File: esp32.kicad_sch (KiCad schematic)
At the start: 34 parts, among them J3 TC2030-IDC, J8 USB_C_Receptacle_USB2.0, Q3 S8050, SW1 GT-TC029B-H025-L1N, SW2 GT-TC029B-H025-L1N, U3 176x320_st7789, U7 SN74AVC4T774, U9 ESP32-S3-WROOM-1, Y1 32.768kHz

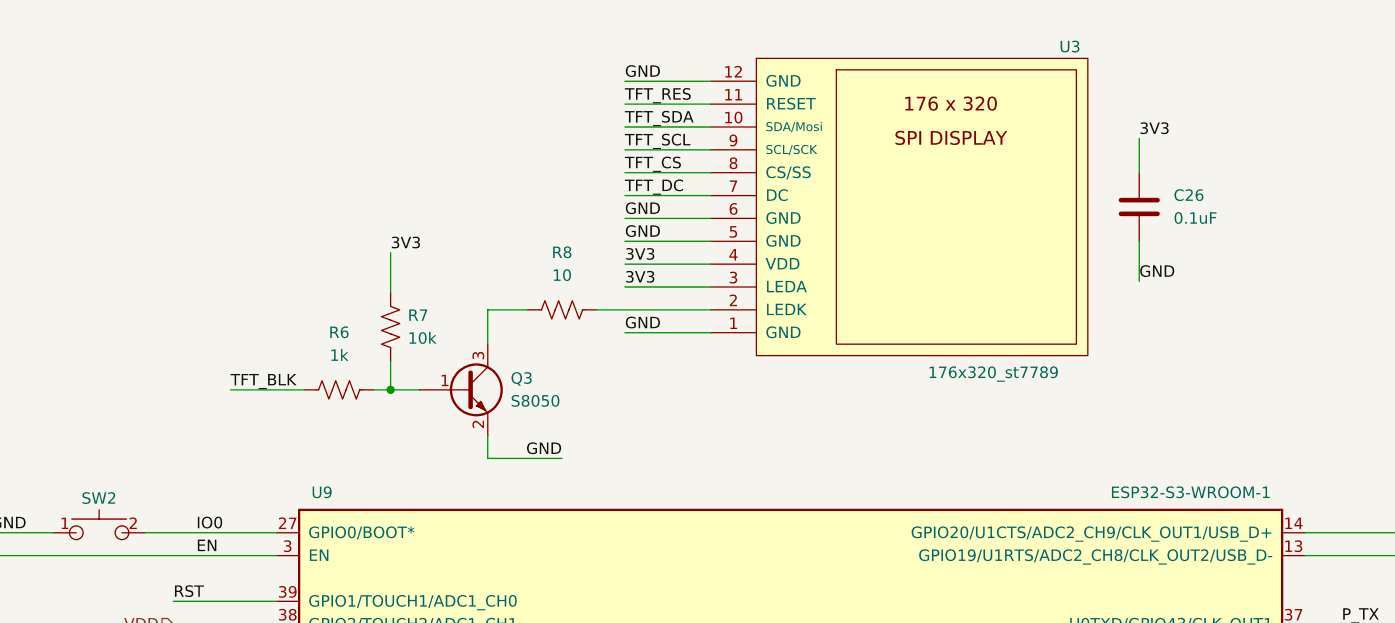
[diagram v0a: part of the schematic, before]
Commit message: replace Q5 with BSS123
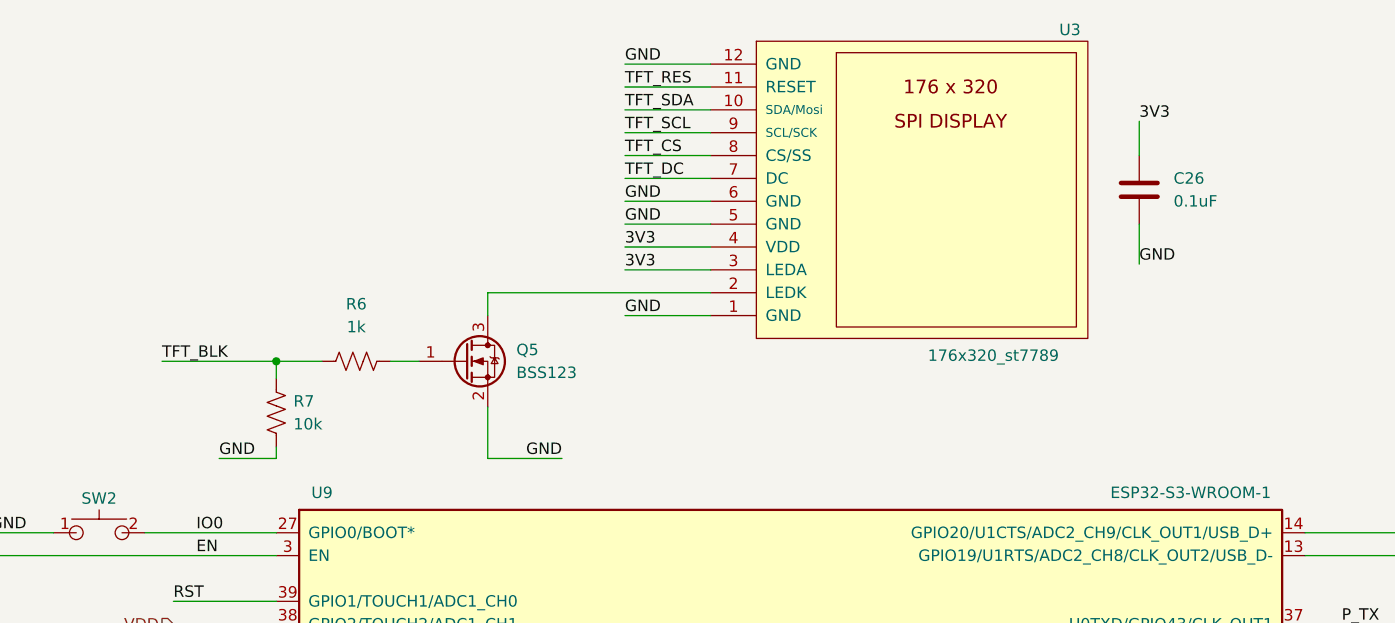
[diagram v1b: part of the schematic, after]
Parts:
- removed Q3: S8050, Package_TO_SOT_SMD:SOT-23-3, symbol Device:Q_NPN_BEC
- removed R8: 10, Resistor_SMD:R_0402_1005Metric, symbol Device:R_US
- added Q5: BSS123, Package_TO_SOT_SMD:SOT-23, symbol Device:Q_NMOS_GSD
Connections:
- net 3V3: no longer R7.2
- net GND: now also R7.1, Q5.2 (S)
- net TFT_BLK: now also R7.2
- net at R6.2: now also Q5.1 (G); no longer R7.1
- net at U3.2 (LEDK): now also Q5.3 (D)
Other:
- moved on the sheet: C26, R6, R7, U3

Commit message: Rough parts placement
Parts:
- TP10, TP11, TP12, TP13, TP14, TP15, TP16, TP8, TP9: footprint TestPoint:TestPoint_Pad_D1.5mm -> TestPoint:TestPoint_Pad_D1.0mm
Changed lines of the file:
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@@
       (effects (font (size 1.27 1.27)) (justify left) hide)
     )
-    (property "Footprint" "TestPoint:TestPoint_Pad_D1.5mm" (at 89.535 163.195 0)
+    (property "Footprint" "TestPoint:TestPoint_Pad_D1.0mm" (at 89.535 163.195 0)
       (effects (font (size 1.27 1.27)) hide)
     )
@@
       (effects (font (size 1.27 1.27)) (justify left) hide)
     )
-    (property "Footprint" "TestPoint:TestPoint_Pad_D1.5mm" (at 62.865 173.355 0)
+    (property "Footprint" "TestPoint:TestPoint_Pad_D1.0mm" (at 62.865 173.355 0)
       (effects (font (size 1.27 1.27)) hide)
     )
@@
       (effects (font (size 1.27 1.27)) (justify left) hide)
     )
-    (property "Footprint" "TestPoint:TestPoint_Pad_D1.5mm" (at 61.595 137.795 0)
+    (property "Footprint" "TestPoint:TestPoint_Pad_D1.0mm" (at 61.595 137.795 0)
       (effects (font (size 1.27 1.27)) hide)
     )
@@
       (effects (font (size 1.27 1.27)) (justify left) hide)
     )
-    (property "Footprint" "TestPoint:TestPoint_Pad_D1.5mm" (at 215.9 159.385 0)
+    (property "Footprint" "TestPoint:TestPoint_Pad_D1.0mm" (at 215.9 159.385 0)
       (effects (font (size 1.27 1.27)) hide)
     )
@@
       (effects (font (size 1.27 1.27)) (justify left) hide)
     )
-    (property "Footprint" "TestPoint:TestPoint_Pad_D1.5mm" (at 244.475 151.765 0)
+    (property "Footprint" "TestPoint:TestPoint_Pad_D1.0mm" (at 244.475 151.765 0)
       (effects (font (size 1.27 1.27)) hide)
     )
@@
       (effects (font (size 1.27 1.27)) (justify left) hide)
     )
-    (property "Footprint" "TestPoint:TestPoint_Pad_D1.5mm" (at 91.44 174.625 0)
+    (property "Footprint" "TestPoint:TestPoint_Pad_D1.0mm" (at 91.44 174.625 0)
       (effects (font (size 1.27 1.27)) hide)
     )
@@
       (effects (font (size 1.27 1.27)) (justify left) hide)
     )
-    (property "Footprint" "TestPoint:TestPoint_Pad_D1.5mm" (at 61.595 134.62 0)
+    (property "Footprint" "TestPoint:TestPoint_Pad_D1.0mm" (at 61.595 134.62 0)
       (effects (font (size 1.27 1.27)) hide)
     )
@@
       (effects (font (size 1.27 1.27)) (justify left) hide)
     )
-    (property "Footprint" "TestPoint:TestPoint_Pad_D1.5mm" (at 215.9 156.845 0)
+    (property "Footprint" "TestPoint:TestPoint_Pad_D1.0mm" (at 215.9 156.845 0)
       (effects (font (size 1.27 1.27)) hide)
     )
@@
       (effects (font (size 1.27 1.27)) (justify left) hide)
     )
-    (property "Footprint" "TestPoint:TestPoint_Pad_D1.5mm" (at 215.9 161.925 0)
-      (effects (font (size 1.27 1.27)) hide)
-    )
+    (property "Footprint" "TestPoint:TestPoint_Pad_D1.0mm" (at 215.9 161.925 0)
+      (effects (font (size 1.27 1.27)) hide)
+    )

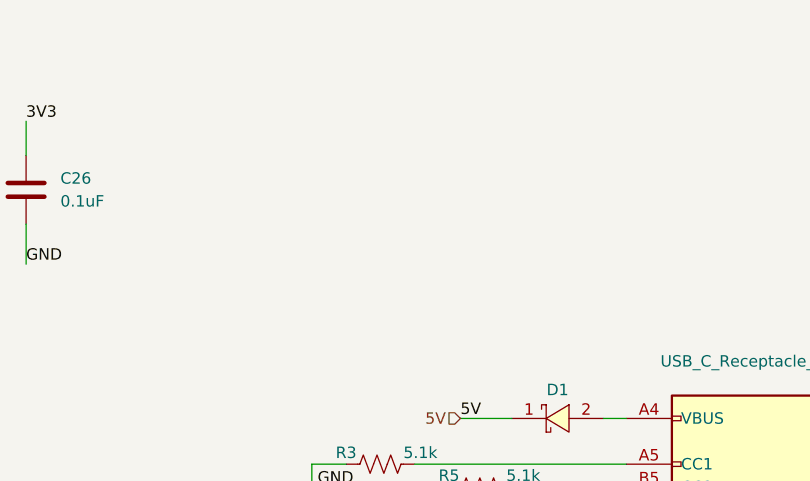
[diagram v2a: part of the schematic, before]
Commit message: add screw terminals, replace OLED display with optional connector
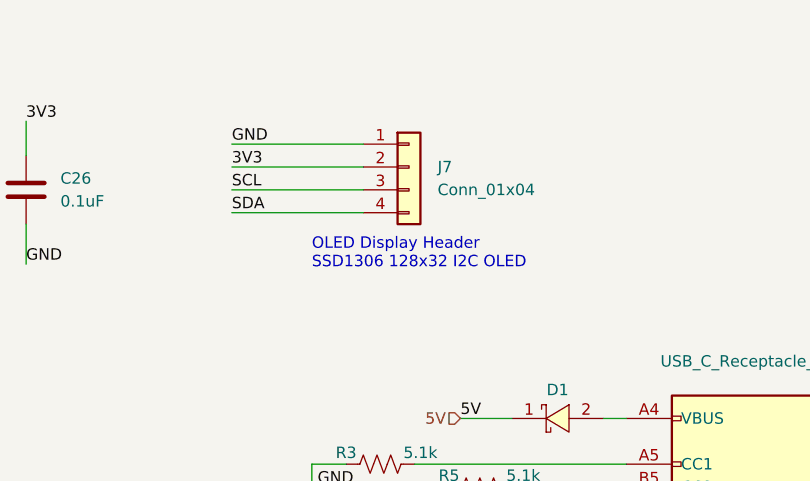
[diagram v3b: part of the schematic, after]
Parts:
- added J7: Conn_01x04, Connector_PinHeader_2.54mm:PinHeader_1x04_P2.54mm_Vertical, symbol Connector_Generic:Conn_01x04
- U3: footprint bitaxe:ST7789-176x320 -> Connector_PinHeader_2.54mm:PinHeader_2x06_P2.54mm_Vertical
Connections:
- net 3V3: now also J7.2 (Pin_2)
- net GND: now also J7.1 (Pin_1)
- net SCL: now also J7.3 (Pin_3)
- net SDA: now also J7.4 (Pin_4)
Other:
- note added: "OLED Display Header SSD1306 128x32 I2C OLED"
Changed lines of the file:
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@@
+    (stroke (width 0) (type default))
+  )
+  (wire (pts (xy 191.77 33.02) (xy 206.375 33.02))
     (stroke (width 0) (type default))
   )
@@
     (stroke (width 0) (type default))
   )
+  (wire (pts (xy 191.77 35.56) (xy 206.375 35.56))
+    (stroke (width 0) (type default))
+  )
   (wire (pts (xy 61.595 132.715) (xy 67.31 132.715))
     (stroke (width 0) (type default))
@@
     (stroke (width 0) (type default))
   )
+  (wire (pts (xy 191.77 30.48) (xy 206.375 30.48))
+    (stroke (width 0) (type default))
+  )
   (wire (pts (xy 111.76 39.37) (xy 121.285 39.37))
     (stroke (width 0) (type default))
@@
   (wire (pts (xy 86.995 172.085) (xy 100.33 172.085))
     (stroke (width 0) (type default))
+  )
+  (wire (pts (xy 191.77 27.94) (xy 206.375 27.94))
+    (stroke (width 0) (type default))
+  )
+  (text "OLED Display Header\nSSD1306 128x32 I2C OLED" (at 200.66 41.91 0)
+    (effects (font (size 1.27 1.27)) (justify left bottom))
   )
   (text "RTC Clock Crystal" (at 231.14 131.445 0)
@@
     (effects (font (size 1.27 1.27)) (justify left bottom))
   )
+  (label "3V3" (at 191.77 30.48 0) (fields_autoplaced)
+    (effects (font (size 1.27 1.27)) (justify left bottom))
+  )
+  (label "GND" (at 191.77 27.94 0) (fields_autoplaced)
+    (effects (font (size 1.27 1.27)) (justify left bottom))
+  )
   (label "TFT_SCL" (at 61.595 91.44 0) (fields_autoplaced)
     (effects (font (size 1.27 1.27)) (justify left bottom))
@@
     (effects (font (size 1.27 1.27)) (justify right bottom))
   )
+  (label "SDA" (at 191.77 35.56 0) (fields_autoplaced)
+    (effects (font (size 1.27 1.27)) (justify left bottom))
+  )
   (label "TFT_DC" (at 111.76 31.75 0) (fields_autoplaced)
     (effects (font (size 1.27 1.27)) (justify left bottom))
@@
   )
   (label "TFT_CS" (at 61.595 93.98 0) (fields_autoplaced)
+    (effects (font (size 1.27 1.27)) (justify left bottom))
+  )
+  (label "SCL" (at 191.77 33.02 0) (fields_autoplaced)
     (effects (font (size 1.27 1.27)) (justify left bottom))
   )
@@
     )
   )
+  (symbol (lib_id "Connector_Generic:Conn_01x04") (at 211.455 30.48 0) (unit 1)
+    (in_bom yes) (on_board yes) (dnp no) (fields_autoplaced)
+    (property "Reference" "J7" (at 214.63 30.48 0)
+      (effects (font (size 1.27 1.27)) (justify left))
+    )
+    (property "Value" "Conn_01x04" (at 214.63 33.02 0)
+      (effects (font (size 1.27 1.27)) (justify left))
+    )
+    (property "Footprint" "Connector_PinHeader_2.54mm:PinHeader_1x04_P2.54mm_Vertical" (at 211.455 30.48 0)
+      (effects (font (size 1.27 1.27)) hide)
+    )
+    (property "Datasheet" "~" (at 211.455 30.48 0)
+      (effects (font (size 1.27 1.27)) hide)
+    )
+    (pin "1")
+    (pin "2")
+    (pin "3")
+    (pin "4")
+    (instances
+      (project "bitaxeUltraHex"
+        (path "/e63e39d7-6ac0-4ffd-8aa3-1841a4541b55/ca857324-2ec8-447e-bd58-90d0c2e6b6d7"
+          (reference "J7") (unit 1)
+        )
+      )
+    )
+  )
   (symbol (lib_id "lcsc:GT-TC029B-H025-L1N") (at 21.59 75.565 0) (unit 1)
     (in_bom yes) (on_board yes) (dnp no) (fields_autoplaced)
@@
       (effects (font (size 1.27 1.27)) (justify left))
     )
-    (property "Footprint" "bitaxe:ST7789-176x320" (at 147.955 53.34 0)
+    (property "Footprint" "Connector_PinHeader_2.54mm:PinHeader_2x06_P2.54mm_Vertical" (at 147.955 53.34 0)
       (effects (font (size 1.524 1.524)) hide)
     )

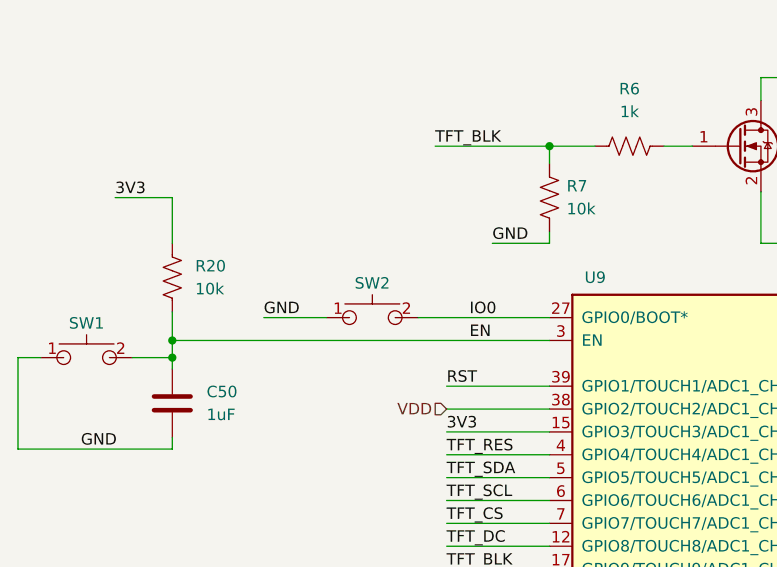
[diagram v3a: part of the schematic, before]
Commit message: More parts placement
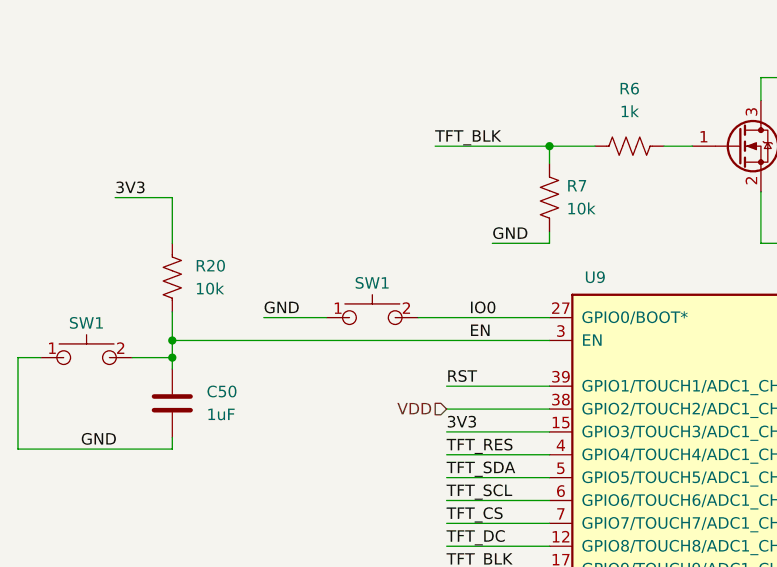
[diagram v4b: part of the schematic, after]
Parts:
- removed SW2: GT-TC029B-H025-L1N, lcsc:SW-SMD_L3.9-W3.0-P4.45, symbol lcsc:GT-TC029B-H025-L1N
- added SW1: EVQ-9P701P, bitaxe:EVQ9P701P-switch, symbol lcsc:GT-TC029B-H025-L1N
- SW1: value GT-TC029B-H025-L1N -> EVQ-9P701P; footprint lcsc:SW-SMD_L3.9-W3.0-P4.45 -> bitaxe:EVQ9P701P-switch; JLC Part Extended Part -> (none); LCSC Part C843669 -> (none); Manufacturer G-Switch(品赞) -> Panasonic; Panasonic PN (none) -> EVQ-9P701P
- U9: footprint bitaxe:ESP32-S3-WROOM-1 -> bitaxe:ESP32-S3-WROOM-1U
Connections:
- net GND: now also SW1.1
- net IO0: now also SW1.2
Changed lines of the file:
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@@
       (effects (font (size 1.27 1.27)))
     )
-    (property "Value" "GT-TC029B-H025-L1N" (at 21.59 71.755 0)
-      (effects (font (size 1.27 1.27)) hide)
-    )
-    (property "Footprint" "lcsc:SW-SMD_L3.9-W3.0-P4.45" (at 21.59 83.185 0)
-      (effects (font (size 1.27 1.27)) hide)
-    )
-    (property "Datasheet" "https://lcsc.com/product-detail/Tactile-Switches_G-Switch-GT-TC029B-H025-L1N_C843669.html" (at 21.59 85.725 0)
-      (effects (font (size 1.27 1.27)) hide)
-    )
-    (property "Manufacturer" "G-Switch(品赞)" (at 21.59 88.265 0)
-      (effects (font (size 1.27 1.27)) hide)
-    )
-    (property "LCSC Part" "C843669" (at 21.59 90.805 0)
-      (effects (font (size 1.27 1.27)) hide)
-    )
-    (property "JLC Part" "Extended Part" (at 21.59 93.345 0)
+    (property "Value" "EVQ-9P701P" (at 21.59 71.755 0)
+      (effects (font (size 1.27 1.27)) hide)
+    )
+    (property "Footprint" "bitaxe:EVQ9P701P-switch" (at 21.59 83.185 0)
+      (effects (font (size 1.27 1.27)) hide)
+    )
+    (property "Datasheet" "https://api.pim.na.industrial.panasonic.com/file_stream/main/fileversion/245500" (at 21.59 85.725 0)
+      (effects (font (size 1.27 1.27)) hide)
+    )
+    (property "Manufacturer" "Panasonic" (at 21.59 88.265 0)
+      (effects (font (size 1.27 1.27)) hide)
+    )
+    (property "Panasonic PN" "EVQ-9P701P" (at 21.59 75.565 0)
       (effects (font (size 1.27 1.27)) hide)
     )
@@
         (path "/e63e39d7-6ac0-4ffd-8aa3-1841a4541b55/ca857324-2ec8-447e-bd58-90d0c2e6b6d7"
           (reference "TP16") (unit 1)
+        )
+      )
+    )
+  )
+  (symbol (lib_id "lcsc:GT-TC029B-H025-L1N") (at 53.34 71.12 0) (unit 1)
+    (in_bom yes) (on_board yes) (dnp no) (fields_autoplaced)
+    (property "Reference" "SW1" (at 53.34 67.31 0)
+      (effects (font (size 1.27 1.27)))
+    )
+    (property "Value" "EVQ-9P701P" (at 53.34 67.31 0)
+      (effects (font (size 1.27 1.27)) hide)
+    )
+    (property "Footprint" "bitaxe:EVQ9P701P-switch" (at 53.34 78.74 0)
+      (effects (font (size 1.27 1.27)) hide)
+    )
+    (property "Datasheet" "https://api.pim.na.industrial.panasonic.com/file_stream/main/fileversion/245500" (at 53.34 81.28 0)
+      (effects (font (size 1.27 1.27)) hide)
+    )
+    (property "Manufacturer" "Panasonic" (at 53.34 83.82 0)
+      (effects (font (size 1.27 1.27)) hide)
+    )
+    (property "Panasonic PN" "EVQ-9P701P" (at 53.34 71.12 0)
+      (effects (font (size 1.27 1.27)) hide)
+    )
+    (pin "1")
+    (pin "2")
+    (instances
+      (project "esp32"
+        (path "/dcd2fc1c-da48-40a9-b97c-5712d9530f4f"
+          (reference "SW1") (unit 1)
+        )
+      )
+      (project "bitaxeUltraHex"
+        (path "/e63e39d7-6ac0-4ffd-8aa3-1841a4541b55/ca857324-2ec8-447e-bd58-90d0c2e6b6d7"
+          (reference "SW2") (unit 1)
         )
       )
@@
     )
   )
-  (symbol (lib_id "lcsc:GT-TC029B-H025-L1N") (at 53.34 71.12 0) (unit 1)
-    (in_bom yes) (on_board yes) (dnp no) (fields_autoplaced)
-    (property "Reference" "SW2" (at 53.34 67.31 0)
-      (effects (font (size 1.27 1.27)))
-    )
-    (property "Value" "GT-TC029B-H025-L1N" (at 53.34 67.31 0)
-      (effects (font (size 1.27 1.27)) hide)
-    )
-    (property "Footprint" "lcsc:SW-SMD_L3.9-W3.0-P4.45" (at 53.34 78.74 0)
-      (effects (font (size 1.27 1.27)) hide)
-    )
-    (property "Datasheet" "https://lcsc.com/product-detail/Tactile-Switches_G-Switch-GT-TC029B-H025-L1N_C843669.html" (at 53.34 81.28 0)
-      (effects (font (size 1.27 1.27)) hide)
-    )
-    (property "Manufacturer" "G-Switch(品赞)" (at 53.34 83.82 0)
-      (effects (font (size 1.27 1.27)) hide)
-    )
-    (property "LCSC Part" "C843669" (at 53.34 86.36 0)
-      (effects (font (size 1.27 1.27)) hide)
-    )
-    (property "JLC Part" "Extended Part" (at 53.34 88.9 0)
-      (effects (font (size 1.27 1.27)) hide)
-    )
-    (pin "1")
-    (pin "2")
-    (instances
-      (project "esp32"
-        (path "/dcd2fc1c-da48-40a9-b97c-5712d9530f4f"
-          (reference "SW2") (unit 1)
-        )
-      )
-      (project "bitaxeUltraHex"
-        (path "/e63e39d7-6ac0-4ffd-8aa3-1841a4541b55/ca857324-2ec8-447e-bd58-90d0c2e6b6d7"
-          (reference "SW2") (unit 1)
-        )
-      )
-    )
-  )
   (symbol (lib_id "bitaxe:ESP32-S3-WROOM-1") (at 128.905 101.6 0) (unit 1)
     (in_bom yes) (on_board yes) (dnp no)
@@
       (effects (font (size 1.27 1.27)))
     )
-    (property "Footprint" "bitaxe:ESP32-S3-WROOM-1" (at 128.905 134.62 0)
-      (effects (font (size 1.27 1.27)) hide)
-    )
+    (property "Footprint" "bitaxe:ESP32-S3-WROOM-1U" (at 128.905 134.62 0)
+      (effects (font (size 1.27 1.27)) hide)
+    )
